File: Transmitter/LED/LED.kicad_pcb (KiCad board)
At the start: 2 copper layers, 50 x 35 mm, 11 parts, among them J1 RFPC-SMA28-F, J2 RFPC-SMA28-F, J4 Vdc

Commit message: Fixed LED pcb
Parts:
- removed J4: Vdc, TerminalBlock_Phoenix:TerminalBlock_Phoenix_MKDS-1,5-2_1x02_P5.00mm_Horizontal
- added J3: Vdc, TerminalBlock_Phoenix:TerminalBlock_Phoenix_MKDS-1,5-2_1x02_P5.00mm_Horizontal, B.Cu at (142.0, 94.0)
- H1, H2, H3: footprint MountingHole:MountingHole_2.7mm_M2.5 -> MountingHole:MountingHole_3.2mm_M3_DIN965
- moved L1 1.00 mm to (159.0, 93.0)
- moved H3 0.16 mm to (181.0, 116.0)
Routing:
- net Net-(J3-Pin_2): track 19.6 -> 15.8 mm
- net Net-(LED1-anode): track 30.5 -> 28.2 mm
- net GND: vias 90 -> 82
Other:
- board text added: "Two layers. PCB core: FR4. No impedance control. No PCB height restrictions."

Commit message: LED corrections finished
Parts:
- C1, C2: value 1uF -> .1uF; footprint Capacitor_SMD:C_0603_1608Metric_Pad1.08x0.95mm_HandSolder -> Capacitor_SMD:C_0402_1005Metric_Pad0.74x0.62mm_HandSolder
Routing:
- net Net-(LED1-anode): track 28.2 -> 30.8 mm
- net GND: vias 82 -> 80
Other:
- board text added: "Two layers. PCB core: FR4. 1 oz cupper layer No impedance control. No PCB height restrictions."
- board text removed: "Two layers. PCB core: FR4. No impedance control. No PCB height restrictions."

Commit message: Last fix Led pcb
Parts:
- H1, H2, H3: value MountingHole -> M3 Mounting hole
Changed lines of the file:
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@@
 			)
 		)
-		(property "Value" "MountingHole"
+		(property "Value" "M3 Mounting hole"
 			(at 0 3.8 0)
 			(layer "F.Fab")
@@
 			)
 		)
-		(property "Description" "744918220 Wurth"
+		(property "Description" "Broadband AC blocking."
 			(at 0 0 90)
 			(unlocked yes)
@@
 			)
 		)
-		(property "Mfr" " Wurth Elektronik "
+		(property "Manufacturer Part Number" "744918220"
 			(at 0 0 90)
 			(unlocked yes)
@@
 			)
 		)
-		(property "Mfr number" "744918220"
+		(property "Mouser Part Number" "710-744918220"
 			(at 0 0 90)
 			(unlocked yes)
@@
 			)
 		)
-		(property "Mouser" "710-744918220"
+		(property "Manufacturer" " Wurth Elektronik "
 			(at 0 0 90)
 			(unlocked yes)
@@
 			)
 		)
-		(property "Value" "MountingHole"
+		(property "Value" "M3 Mounting hole"
 			(at 0 3.8 0)
 			(layer "F.Fab")
@@
 			)
 		)
-		(property "Value" "MountingHole"
+		(property "Value" "M3 Mounting hole"
 			(at 0 3.8 0)
 			(layer "F.Fab")
@@
 			)
 		)
-		(property "Datasheet" ""
+		(property "Datasheet" "https://datasheets.kyocera-avx.com/530L.pdf"
 			(at 0 0 90)
 			(unlocked yes)
@@
 			)
 		)
-		(property "Description" "broadband DC blocking"
+		(property "Description" "Broadband DC blocking."
 			(at 0 0 90)
 			(unlocked yes)
@@
 			)
 		)
-		(property "Mfr" "KYOCERA AVX"
+		(property "Manufacturer Part Number" "530L104KT16"
 			(at 0 0 90)
 			(unlocked yes)
@@
 			)
 		)
-		(property "Mfr number" "530L104KT16"
+		(property "Mouser Part Number" " 581-530L104KT16 "
 			(at 0 0 90)
 			(unlocked yes)
@@
 			)
 		)
-		(property "Mouser" " 581-530L104KT16 "
+		(property "Manufacturer" "KYOCERA AVX"
 			(at 0 0 90)
 			(unlocked yes)
@@
 			)
 		)
-		(property "Datasheet" ""
+		(property "Datasheet" "https://datasheets.kyocera-avx.com/530L.pdf"
 			(at 0 0 90)
 			(unlocked yes)
@@
 			)
 		)
-		(property "Description" "broadband DC blocking"
+		(property "Description" "Broadband DC blocking."
 			(at 0 0 90)
 			(unlocked yes)
@@
 			)
 		)
-		(property "Mfr" "KYOCERA AVX"
+		(property "Manufacturer Part Number" "530L104KT16"
 			(at 0 0 90)
 			(unlocked yes)
@@
 			)
 		)
-		(property "Mfr number" "530L104KT16"
+		(property "Mouser Part Number" " 581-530L104KT16 "
 			(at 0 0 90)
 			(unlocked yes)
@@
 			)
 		)
-		(property "Mouser" " 581-530L104KT16 "
+		(property "Manufacturer" "KYOCERA AVX"
 			(at 0 0 90)
 			(unlocked yes)
@@
 		(sheetname "Root")
 		(sheetfile "LED.kicad_sch")
-		(attr through_hole)
+		(attr through_hole exclude_from_bom)
 		(fp_line
 			(start -2.3 -4.9)
@@
 			)
 		)
-		(property "Mfr" "Global Connector Technology (GCT)"
+		(property "Manufacturer Part Number" "RFPC-SMA28-F"
 			(at 0 0 90)
 			(unlocked yes)
@@
 			)
 		)
-		(property "Mfr number" "RFPC-SMA28-F"
+		(property "Mouser Part Number" "640-RFPCSMA28F "
 			(at 0 0 90)
 			(unlocked yes)
@@
 			)
 		)
-		(property "Mouser" "640-RFPCSMA28F "
+		(property "Manufacturer" "Global Connector Technology (GCT)"
 			(at 0 0 90)
 			(unlocked yes)
@@
 			)
 		)
-		(property "Mfr" "Global Connector Technology (GCT)"
+		(property "Manufacturer Part Number" "RFPC-SMA28-F"
 			(at 0 0 90)
 			(unlocked yes)
@@
 			)
 		)
-		(property "Mfr number" "RFPC-SMA28-F"
+		(property "Mouser Part Number" "640-RFPCSMA28F "
 			(at 0 0 90)
 			(unlocked yes)
@@
 			)
 		)
-		(property "Mouser" "640-RFPCSMA28F "
+		(property "Manufacturer" "Global Connector Technology (GCT)"
 			(at 0 0 90)
 			(unlocked yes)
@@
 		(net_name "Net-(LED1-anode)")
 		(layer "F.Cu")
-		(name "$teardrop_track$")
+		(name "$teardrop_padvia$")
 		(hatch full 0.1)
-		(priority 30002)
+		(priority 30001)
 		(attr
 			(teardrop
-				(type track_end)
+				(type padvia)
 			)
 		)
@@
 		(polygon
 			(pts
-				(xy 152.500905 106.750781) (xy 152.500905 107.250781) (xy 153.90592 108.000342) (xy 155.001781 107)
-				(xy 153.905235 106.000342)
+				(xy 150.488833 107.250781) (xy 150.488833 106.750781) (xy 149.947127 107.065) (xy 149.999 107.4325)
+				(xy 150.31 107.571616)
 			)
 		)
@@
 		(net_name "Net-(LED1-anode)")
 		(layer "F.Cu")
-		(hatch edge 0.5)
-		(priority 10)
+		(name "$teardrop_track$")
+		(hatch full 0.1)
+		(priority 30002)
+		(attr
+			(teardrop
+				(type track_end)
+			)
+		)
 		(connect_pads yes
-			(clearance 0.5)
+			(clearance 0)
 		)
-		(min_thickness 0.1)
+		(min_thickness 0.0254)
 		(filled_areas_thickness no)
 		(fill yes
@@
 		(polygon
 			(pts
-				(xy 149.7 107.2) (xy 148.6 105.4) (xy 151.4 105.4) (xy 150.3 107.2)
+				(xy 152.500905 106.750781) (xy 152.500905 107.250781) (xy 153.90592 108.000342) (xy 155.001781 107)
+				(xy 153.905235 106.000342)
 			)
 		)
@@
 		(net_name "Net-(LED1-anode)")
 		(layer "F.Cu")
-		(name "$teardrop_padvia$")
-		(hatch full 0.1)
-		(priority 30006)
-		(attr
-			(teardrop
-				(type padvia)
-			)
-		)
+		(hatch edge 0.5)
+		(priority 10)
 		(connect_pads yes
-			(clearance 0)
+			(clearance 0.5)
 		)
-		(min_thickness 0.0254)
+		(min_thickness 0.1)
 		(filled_areas_thickness no)
 		(fill yes
@@
 		(polygon
 			(pts
-				(xy 150.488833 107.250781) (xy 150.488833 106.750781) (xy 149.947127 107.065) (xy 149.999 107.4325)
-				(xy 150.31 107.571616)
+				(xy 149.7 107.2) (xy 148.6 105.4) (xy 151.4 105.4) (xy 150.3 107.2)
 			)
 		)
@@
 	)
 	(zone
-		(net 2)
-		(net_name "Net-(J1-In)")
+		(net 5)
+		(net_name "Net-(LED1-anode)")
 		(layer "F.Cu")
 		(name "$teardrop_padvia$")
 		(hatch full 0.1)
-		(priority 30003)
+		(priority 30000)
 		(attr
 			(teardrop
@@
 		(polygon
 			(pts
-				(xy 170.5 112.975) (xy 169.5 112.975) (xy 169.053023 114.607749) (xy 170 115.001) (xy 170.946977 114.607749)
+				(xy 169.508085 106.75) (xy 169.508085 107.25) (xy 169.69 107.572033) (xy 170.001 107.4325) (xy 170.052189 107.065)
 			)
 		)
 	)
 	(zone
-		(net 3)
-		(net_name "Net-(J2-In)")
+		(net 2)
+		(net_name "Net-(J1-In)")
 		(layer "F.Cu")
 		(name "$teardrop_padvia$")
 		(hatch full 0.1)
-		(priority 30004)
+		(priority 30000)
 		(attr
 			(teardrop
@@
 		(polygon
 			(pts
-				(xy 150.5 112.975) (xy 149.5 112.975) (xy 149.053023 114.607749) (xy 150 115.001) (xy 150.946977 114.607749)
+				(xy 170.5 112.975) (xy 169.5 112.975) (xy 169.053023 114.607749) (xy 170 115.001) (xy 170.946977 114.607749)
 			)
 		)
@@
 	)
 	(zone
-		(net 5)
-		(net_name "Net-(LED1-anode)")
+		(net 3)
+		(net_name "Net-(J2-In)")
 		(layer "F.Cu")
 		(name "$teardrop_padvia$")
 		(hatch full 0.1)
-		(priority 30005)
+		(priority 30001)
 		(attr
 			(teardrop
@@
 		(polygon
 			(pts
-				(xy 169.508085 106.75) (xy 169.508085 107.25) (xy 169.69 107.572033) (xy 170.001 107.4325) (xy 170.052189 107.065)
+				(xy 150.5 112.975) (xy 149.5 112.975) (xy 149.053023 114.607749) (xy 150 115.001) (xy 150.946977 114.607749)
 			)
 		)

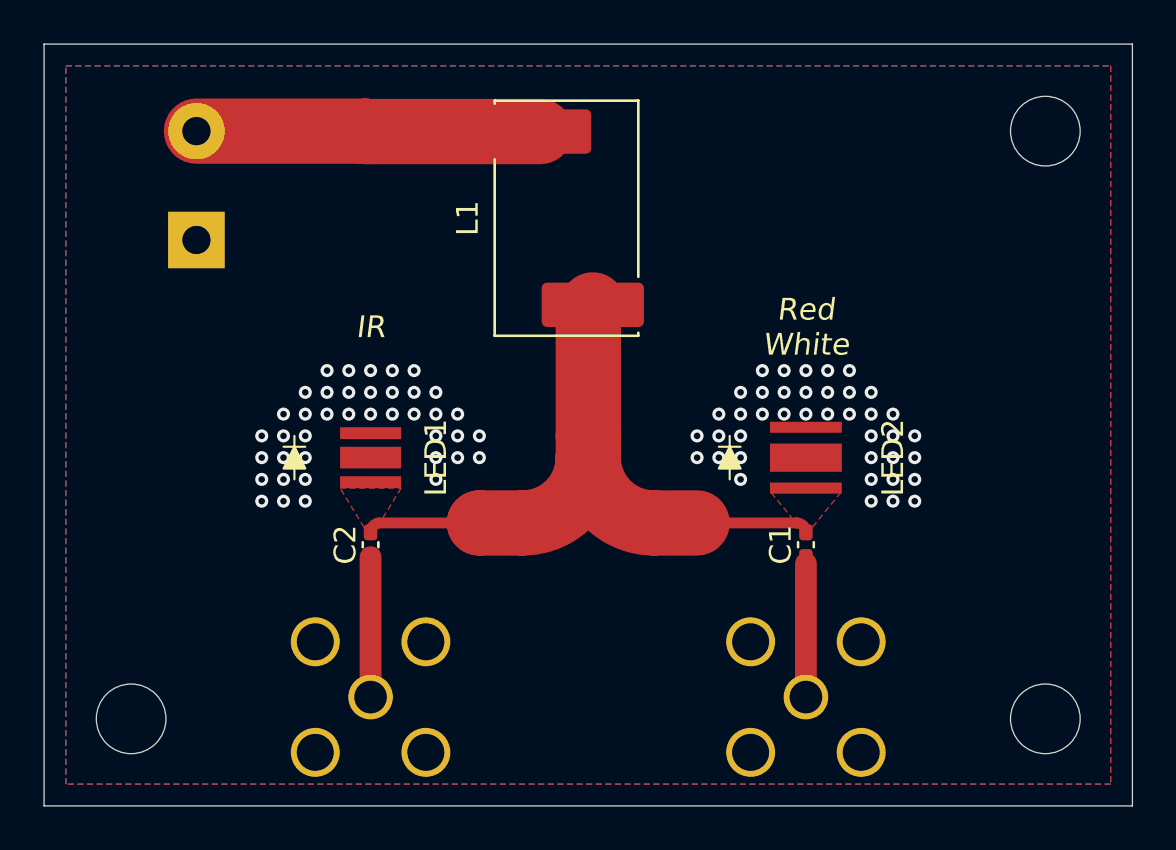
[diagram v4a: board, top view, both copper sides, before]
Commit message: Capacitors descriptors fixed, some fix to DRC
Capacitors descriptors fixed, some fix to DRC
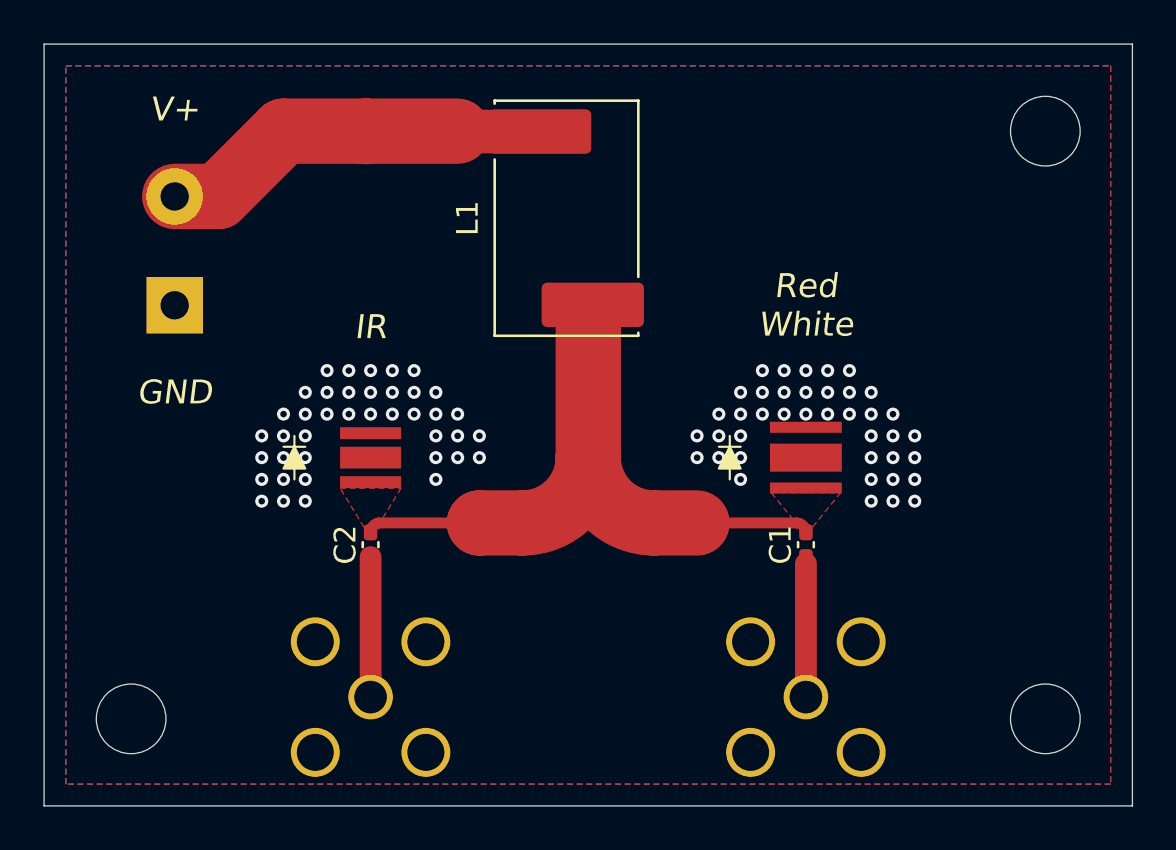
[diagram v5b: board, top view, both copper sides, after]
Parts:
- moved J3 3.16 mm to (141.0, 97.0)
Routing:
- net Net-(J3-Pin_2): track 15.8 -> 18.1 mm
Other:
- board text added: "GND"
- board text added: "V+"
- board text removed: "Vdc"
